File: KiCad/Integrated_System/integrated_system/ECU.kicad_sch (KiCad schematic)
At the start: 49 parts, among them J1 Jack-DC, J2 Fan 1, J3 Fan 2, J4 Fan 3, Q1 BSS138, Q2 BSS138, Q3 BSS138, SW1 SW_SPDT, SW2 SW_SPDT, SW3 SW_Push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

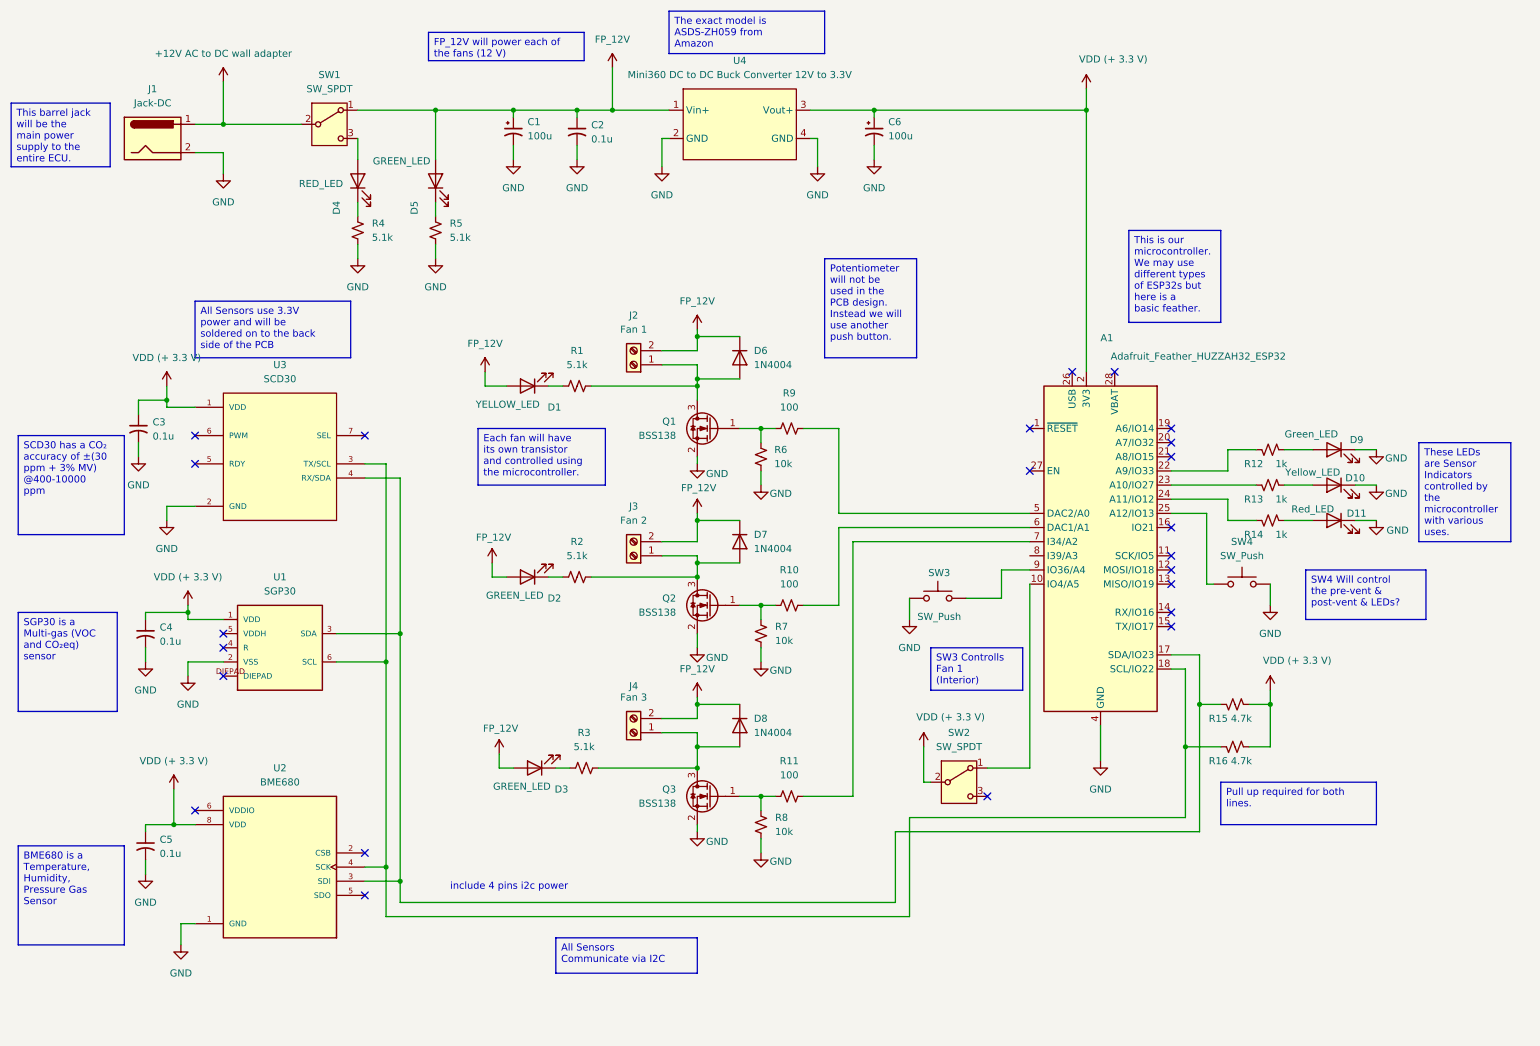
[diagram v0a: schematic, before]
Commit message: added zero ojm resistors and testpoints
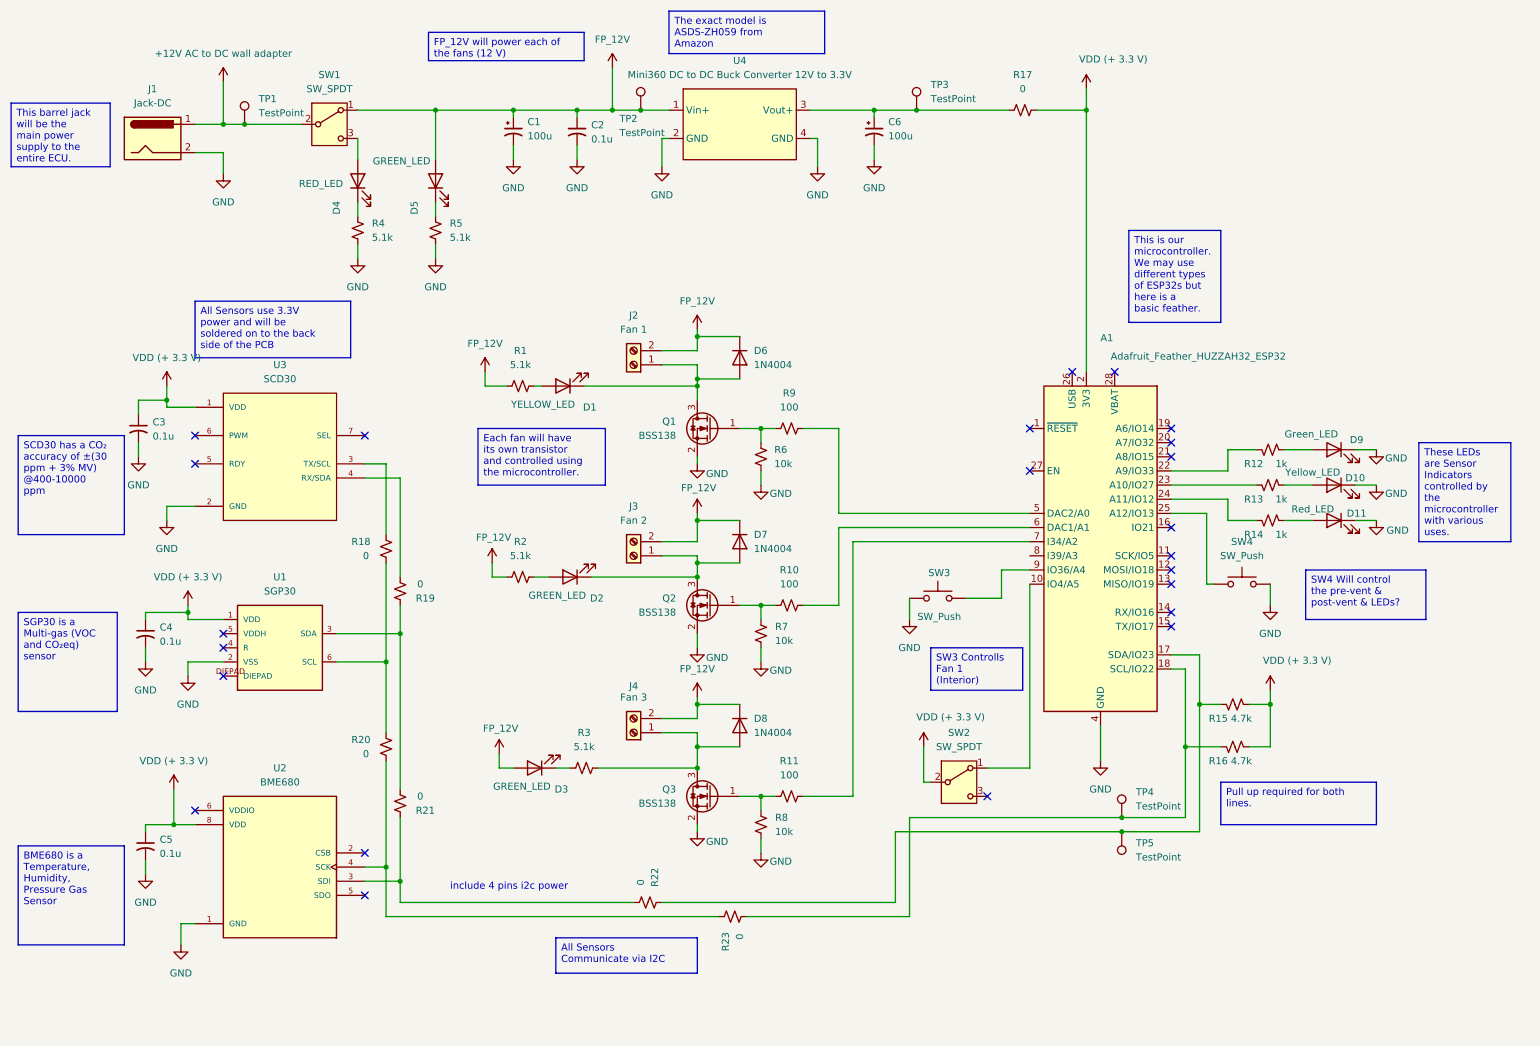
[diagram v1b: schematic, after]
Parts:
- added R17, R18, R19, R20, R21, R22, R23: 0, Resistor_SMD:R_1206_3216Metric_Pad1.30x1.75mm_HandSolder, symbol Device:R_Small_US
- added TP1, TP2, TP3, TP4, TP5: TestPoint, Connector_Pin:Pin_D0.7mm_L6.5mm_W1.8mm_FlatFork, symbol Connector:TestPoint
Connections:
- net +12V AC to DC wall adapter: now also TP1.1
- net FP_12V: now also R1.1, R2.1, TP2.1; no longer D1.2 (A), D2.2 (A)
- net VDD (+ 3.3 V): now also R17.2; no longer C6.1, U4.3 (Vout+)
- net at D6.2 (A), J2.1 (Pin_1), Q1.3 (D): now also D1.1 (K); no longer R1.2
- net at D2.1 (K): now also D7.2 (A), J3.1 (Pin_1), Q2.3 (D); no longer R2.1
- new net: A1.18 (SCL/IO22), R16.2, R23.2, TP4.1
- new net: R19.1, R21.2, U1.3 (SDA)
- new net: R18.2, R20.1, U1.6 (SCL)
- new net: A1.17 (SDA/IO23), R15.2, R22.1, TP5.1
- new net: R21.1, R22.2, U2.3 (SDI)
- new net: D1.2 (A), R1.2
- new net: D2.2 (A), R2.2
- new net: R18.1, U3.3 (TX/SCL)
- new net: R19.2, U3.4 (RX/SDA)
- new net: C6.1, R17.1, TP3.1, U4.3 (Vout+)
- new net: R20.2, R23.1, U2.4 (SCK)
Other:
- moved on the sheet: D1, D2, R1, R2

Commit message: added I2C extension
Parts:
- removed R18, R19, R20, R21, R22, R23: 0, Resistor_SMD:R_1206_3216Metric_Pad1.30x1.75mm_HandSolder, symbol Device:R_Small_US
- added C7: 0.1u, Capacitor_SMD:C_1206_3216Metric_Pad1.33x1.80mm_HandSolder, symbol Device:C_Small_US
- added J5: Conn_01x04, Connector_PinSocket_2.54mm:PinSocket_1x04_P2.54mm_Vertical, symbol Connector_Generic:Conn_01x04
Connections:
- net GND: now also C7.2, J5.3 (Pin_3)
- net VDD (+ 3.3 V): now also C7.1, J5.4 (Pin_4)
- net at A1.18 (SCL/IO22), R16.2, TP4.1: now also U1.6 (SCL), U2.4 (SCK), U3.3 (TX/SCL), J5.2 (Pin_2)
- net at U1.3 (SDA): now also A1.17 (SDA/IO23), R15.2, TP5.1, U2.3 (SDI), U3.4 (RX/SDA), J5.1 (Pin_1)
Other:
- note removed: "include 4 pins i2c power"

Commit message: redesign
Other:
- moved on the sheet: C7
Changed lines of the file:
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@@
 	(text_box "This is our microcontroller. We may use different types of ESP32s but here is a basic feather."
 		(exclude_from_sim no)
-		(at 213.36 53.34 0)
+		(at 175.26 78.74 0)
 		(size 16.51 16.51)
 		(margins 0.9525 0.9525 0.9525 0.9525)
@@
 	)
 	(junction
+		(at 148.59 185.42)
+		(diameter 0)
+		(color 0 0 0 0)
+	)
+	(junction
 		(at 135.89 176.53)
 		(diameter 0)
@@
 	)
 	(junction
-		(at 148.59 182.88)
-		(diameter 0)
-		(color 0 0 0 0)
-	)
-	(junction
 		(at 135.89 115.57)
 		(diameter 0)
@@
 	(wire
 		(pts
-			(xy 163.83 184.15) (xy 163.83 182.88)
-		)
-		(stroke
-			(width 0)
-			(type default)
-		)
-	)
-	(wire
-		(pts
 			(xy 135.89 113.03) (xy 143.51 113.03)
 		)
@@
 	(wire
 		(pts
+			(xy 148.59 193.04) (xy 148.59 194.31)
+		)
+		(stroke
+			(width 0)
+			(type default)
+		)
+	)
+	(wire
+		(pts
 			(xy 135.89 81.28) (xy 135.89 83.82)
 		)
@@
 	(wire
 		(pts
-			(xy 100.33 147.32) (xy 100.33 149.86)
+			(xy 148.59 185.42) (xy 148.59 187.96)
 		)
 		(stroke
@@
 	(wire
 		(pts
-			(xy 43.18 177.8) (xy 45.72 177.8)
+			(xy 100.33 147.32) (xy 100.33 149.86)
 		)
 		(stroke
@@
 	(wire
 		(pts
-			(xy 231.14 96.52) (xy 231.14 92.71)
+			(xy 43.18 177.8) (xy 45.72 177.8)
 		)
 		(stroke
@@
 	(wire
 		(pts
-			(xy 148.59 182.88) (xy 163.83 182.88)
+			(xy 231.14 96.52) (xy 231.14 92.71)
 		)
 		(stroke
@@
 	(wire
 		(pts
-			(xy 163.83 189.23) (xy 163.83 191.77)
-		)
-		(stroke
-			(width 0)
-			(type default)
-		)
-	)
-	(wire
-		(pts
 			(xy 106.68 81.28) (xy 107.95 81.28)
 		)
@@
 	(symbol
 		(lib_id "Device:C_Small_US")
-		(at 163.83 186.69 0)
+		(at 148.59 190.5 0)
 		(unit 1)
 		(exclude_from_sim no)
@@
 		(fields_autoplaced yes)
 		(property "Reference" "C7"
-			(at 166.37 185.5469 0)
+			(at 151.13 189.3569 0)
 			(effects
 				(font
@@
 		)
 		(property "Value" "0.1u"
-			(at 166.37 188.0869 0)
+			(at 151.13 191.8969 0)
 			(effects
 				(font
@@
 		)
 		(property "Footprint" "Capacitor_SMD:C_1206_3216Metric_Pad1.33x1.80mm_HandSolder"
-			(at 163.83 186.69 0)
+			(at 148.59 190.5 0)
 			(effects
 				(font
@@
 		)
 		(property "Datasheet" ""
-			(at 163.83 186.69 0)
+			(at 148.59 190.5 0)
 			(effects
 				(font
@@
 		)
 		(property "Description" "capacitor, small US symbol"
-			(at 163.83 186.69 0)
+			(at 148.59 190.5 0)
 			(effects
 				(font
@@
 	(symbol
 		(lib_id "power:GND")
-		(at 163.83 191.77 0)
+		(at 148.59 194.31 0)
 		(unit 1)
 		(exclude_from_sim no)
@@
 		(dnp no)
 		(property "Reference" "#PWR014"
-			(at 163.83 198.12 0)
+			(at 148.59 200.66 0)
 			(effects
 				(font
@@
 		)
 		(property "Value" "GND"
-			(at 167.894 193.294 0)
+			(at 152.654 195.834 0)
 			(effects
 				(font
@@
 		)
 		(property "Footprint" ""
-			(at 163.83 191.77 0)
+			(at 148.59 194.31 0)
 			(effects
 				(font
@@
 		)
 		(property "Datasheet" ""
-			(at 163.83 191.77 0)
+			(at 148.59 194.31 0)
 			(effects
 				(font
@@
 		)
 		(property "Description" "Power symbol creates a global label with name \"GND\" , ground"
-			(at 163.83 191.77 0)
+			(at 148.59 194.31 0)
 			(effects
 				(font
@@
 		)
 		(property "Value" "GND"
-			(at 144.78 190.5 0)
+			(at 141.224 193.802 0)
 			(effects
 				(font

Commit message: small adjustments
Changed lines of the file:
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@@
 		)
 	)
+	(text_box "Might do a switch instead of a zero ohm resistor to bifuracte the power to the ESP32"
+		(exclude_from_sim no)
+		(at 180.34 34.29 0)
+		(size 21.59 12.7)
+		(margins 0.9525 0.9525 0.9525 0.9525)
+		(stroke
+			(width 0)
+			(type solid)
+		)
+		(fill
+			(type none)
+		)
+		(effects
+			(font
+				(size 1.27 1.27)
+			)
+			(justify left top)
+		)
+	)
 	(text_box "The exact model is ASDS-ZH059 from Amazon"
 		(exclude_from_sim no)
@@
 		(on_board yes)
 		(dnp no)
-		(fields_autoplaced yes)
 		(property "Reference" "TP5"
 			(at 214.63 163.3219 0)
@@
 		)
 		(property "Value" "TestPoint"
-			(at 214.63 165.8619 0)
+			(at 202.184 163.068 0)
 			(effects
 				(font

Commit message: title
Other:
- company: OSSEM -> OSSEM (Open-Source Smart Espresso Machine)
- title: Integrated System -> Integrated ECU System
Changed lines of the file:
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@@
 	(paper "A4")
 	(title_block
-		(title "Integrated System")
-		(date "2026-04-22")
-		(rev "1.3")
-		(company "OSSEM")
+		(title "Integrated ECU System")
+		(date "2026-04-23")
+		(rev "1.4")
+		(company "OSSEM (Open-Source Smart Espresso Machine)")
+		(comment 1 "EE Hardware Engineers: David Mazhnikov, Roman Sulza")
 	)
 	(text_box "These LEDs are Sensor Indicators controlled by the microcontroller with various uses."

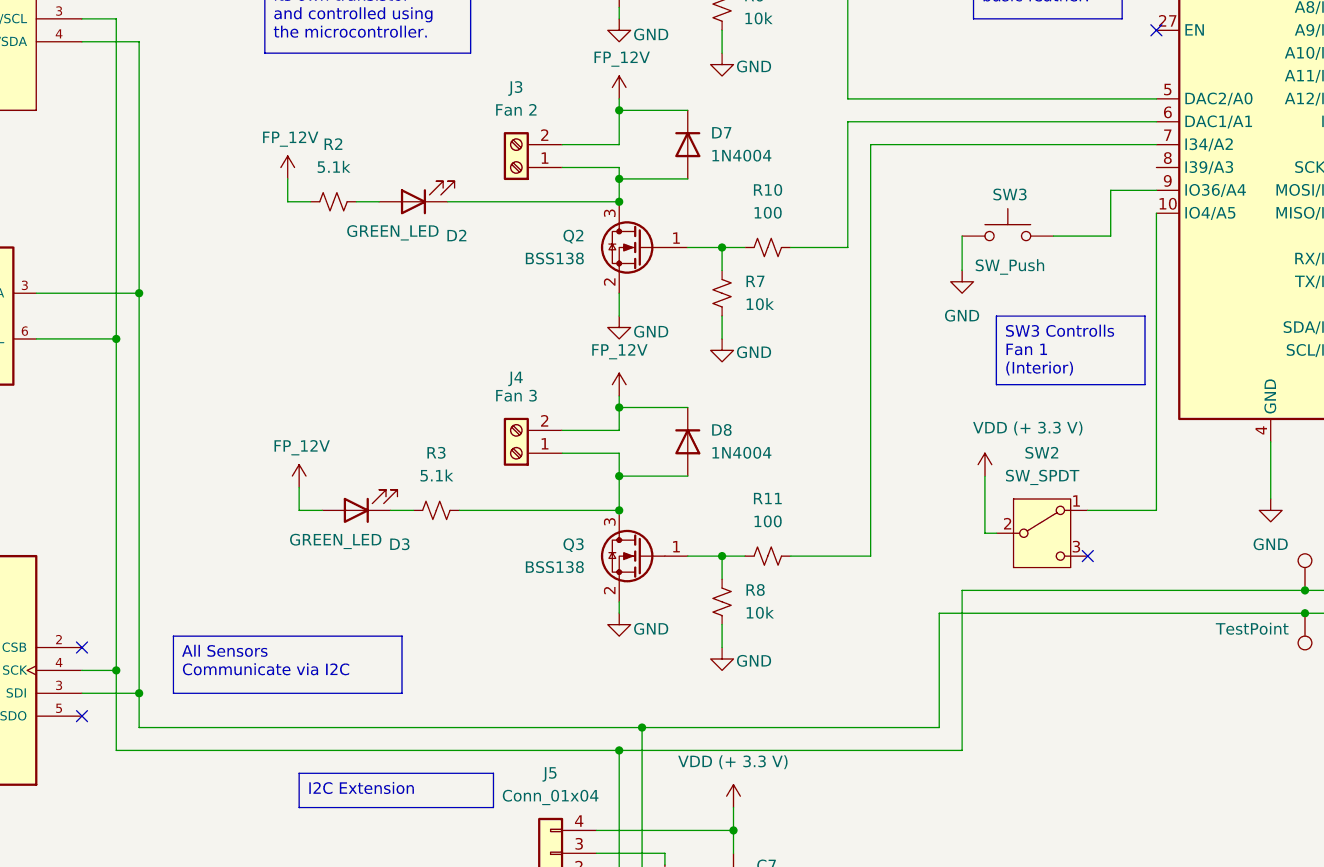
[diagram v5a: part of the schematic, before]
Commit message: Routing Complete
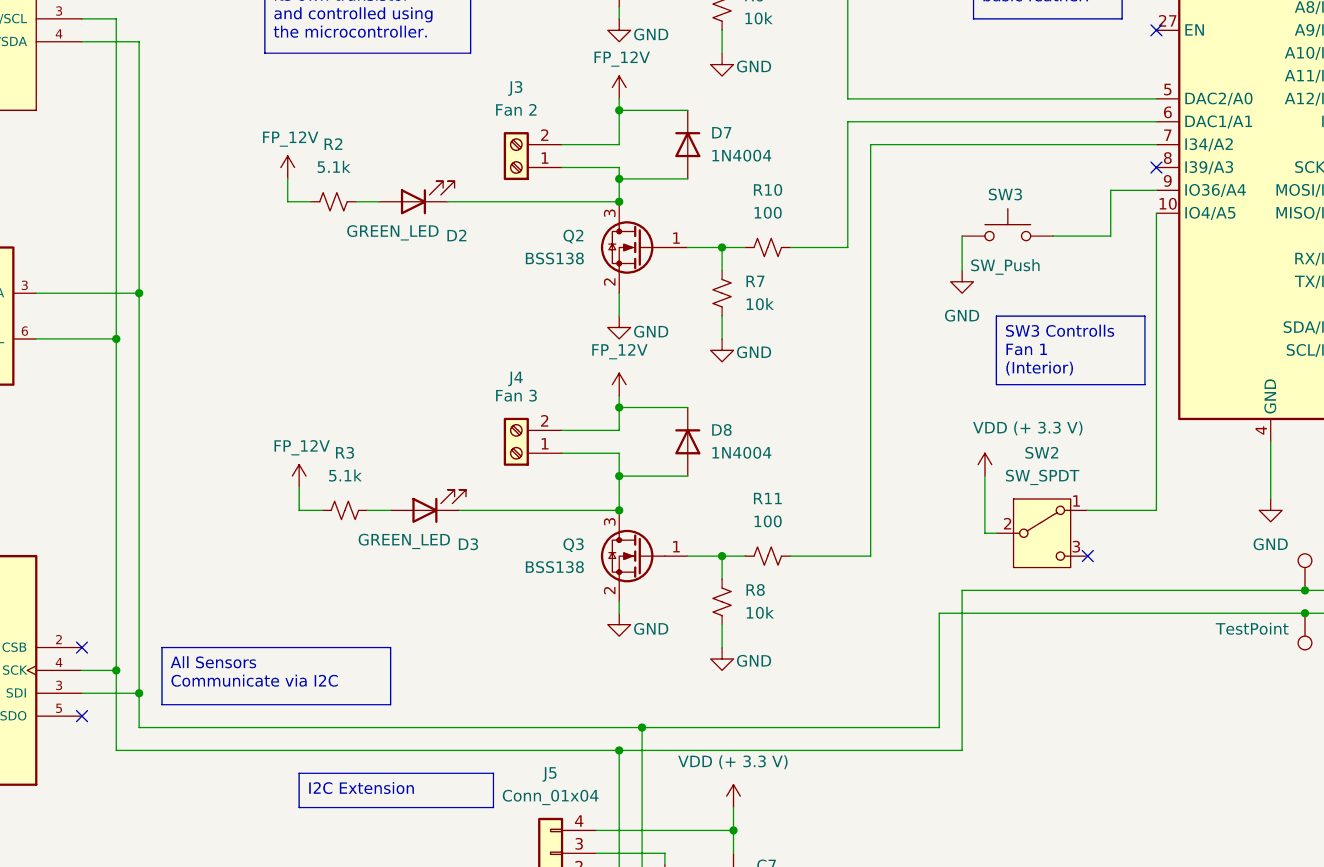
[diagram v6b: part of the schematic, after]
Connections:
- net FP_12V: now also R3.1; no longer D3.2 (A)
- net GND: now also SW3.2; no longer SW3.1
- net at D8.2 (A), J4.1 (Pin_1), Q3.3 (D): now also D3.1 (K); no longer R3.2
- net at A1.9 (IO36/A4): now also SW3.1; no longer SW3.2
- new net: D3.2 (A), R3.2
- no-connect marks 23 -> 24
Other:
- moved on the sheet: D3, R3
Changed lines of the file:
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@@
 	(text_box "All Sensors Communicate via I2C"
 		(exclude_from_sim no)
-		(at 86.36 163.83 0)
+		(at 85.09 165.1 0)
 		(size 25.4 6.35)
 		(margins 0.9525 0.9525 0.9525 0.9525)
@@
 	)
 	(no_connect
+		(at 195.58 111.76)
+	)
+	(no_connect
 		(at 195.58 96.52)
 	)
@@
 	(wire
 		(pts
-			(xy 110.49 149.86) (xy 113.03 149.86)
-		)
-		(stroke
-			(width 0)
-			(type default)
-		)
-	)
-	(wire
-		(pts
 			(xy 129.54 77.47) (xy 135.89 77.47)
 		)
@@
 	(wire
 		(pts
-			(xy 195.58 149.86) (xy 195.58 116.84)
-		)
-		(stroke
-			(width 0)
-			(type default)
-		)
-	)
-	(wire
-		(pts
 			(xy 148.59 182.88) (xy 148.59 185.42)
 		)
@@
 	(wire
 		(pts
+			(xy 195.58 116.84) (xy 195.58 149.86)
+		)
+		(stroke
+			(width 0)
+			(type default)
+		)
+	)
+	(wire
+		(pts
 			(xy 161.29 120.65) (xy 161.29 106.68)
 		)
@@
 	(wire
 		(pts
+			(xy 107.95 149.86) (xy 110.49 149.86)
+		)
+		(stroke
+			(width 0)
+			(type default)
+		)
+	)
+	(wire
+		(pts
 			(xy 135.89 176.53) (xy 80.01 176.53)
 		)
@@
 		(lib_id "Switch:SW_Push")
 		(at 179.07 119.38 0)
+		(mirror y)
 		(unit 1)
 		(exclude_from_sim no)
@@
 		(dnp no)
 		(property "Reference" "SW3"
-			(at 179.324 114.808 0)
+			(at 178.816 114.808 0)
 			(effects
 				(font
@@
 		)
 		(property "Value" "SW_Push"
-			(at 179.324 122.682 0)
+			(at 178.816 122.682 0)
 			(effects
 				(font
@@
 	(symbol
 		(lib_id "Device:LED")
-		(at 106.68 149.86 180)
+		(at 114.3 149.86 180)
 		(unit 1)
 		(exclude_from_sim no)
@@
 		(dnp no)
 		(property "Reference" "D3"
-			(at 111.506 153.67 0)
+			(at 119.126 153.67 0)
 			(effects
 				(font
@@
 		)
 		(property "Value" "GREEN_LED"
-			(at 104.394 153.162 0)
+			(at 112.014 153.162 0)
 			(effects
 				(font
@@
 		)
 		(property "Footprint" "LED_SMD:LED_1206_3216Metric_Pad1.42x1.75mm_HandSolder"
-			(at 106.68 149.86 0)
+			(at 114.3 149.86 0)
 			(effects
 				(font
@@
 		)
 		(property "Datasheet" "~"
-			(at 106.68 149.86 0)
+			(at 114.3 149.86 0)
 			(effects
 				(font
@@
 		)
 		(property "Description" "Light emitting diode"
-			(at 106.68 149.86 0)
+			(at 114.3 149.86 0)
 			(effects
 				(font
@@
 		)
 		(property "Sim.Pins" "1=K 2=A"
-			(at 106.68 149.86 0)
+			(at 114.3 149.86 0)
 			(effects
 				(font
@@
 				)
 			)
-			(project "integrated_system"
-				(path "/e09e0073-4b34-4087-926d-a963f587ec36/d64a58e5-7375-438d-b343-064b897cc797"
-					(reference "D?")
-					(unit 1)
-				)
-			)
 		)
 	)
@@
 	(symbol
 		(lib_id "Device:R_Small_US")
-		(at 115.57 149.86 90)
+		(at 105.41 149.86 90)
 		(unit 1)
 		(exclude_from_sim no)
@@
 		(fields_autoplaced yes)
 		(property "Reference" "R3"
-			(at 115.57 143.51 90)
+			(at 105.41 143.51 90)
 			(effects
 				(font
@@
 		)
 		(property "Value" "5.1k"
-			(at 115.57 146.05 90)
+			(at 105.41 146.05 90)
 			(effects
 				(font
@@
 		)
 		(property "Footprint" "Resistor_SMD:R_1206_3216Metric_Pad1.30x1.75mm_HandSolder"
-			(at 115.57 149.86 0)
+			(at 105.41 149.86 0)
 			(effects
 				(font
@@
 		)
 		(property "Datasheet" "~"
-			(at 115.57 149.86 0)
+			(at 105.41 149.86 0)
 			(effects
 				(font
@@
 		)
 		(property "Description" "Resistor, small US symbol"
-			(at 115.57 149.86 0)
+			(at 105.41 149.86 0)
 			(effects
 				(font
@@
 				)
 			)
-			(project "integrated_system"
-				(path "/e09e0073-4b34-4087-926d-a963f587ec36/d64a58e5-7375-438d-b343-064b897cc797"
-					(reference "R?")
-					(unit 1)
-				)
-			)
 		)
 	)
@@
 		(on_board yes)
 		(dnp no)
-		(fields_autoplaced yes)
 		(property "Reference" "J3"
 			(at 124.46 102.87 0)
@@
 		(on_board yes)
 		(dnp no)
-		(fields_autoplaced yes)
 		(property "Reference" "SW2"
 			(at 182.88 143.51 0)

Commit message: headers
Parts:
- removed J5: Conn_01x04, Connector_PinSocket_2.54mm:PinSocket_1x04_P2.54mm_Vertical, symbol Connector_Generic:Conn_01x04
- added J6: Conn_02x04_Counter_Clockwise, Connector_PinSocket_2.54mm:PinSocket_2x04_P2.54mm_Vertical, symbol Connector_Generic:Conn_02x04_Counter_Clockwise
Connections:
- net GND: now also J6.5 (Pin_5), J6.6 (Pin_6)
- net VDD (+ 3.3 V): now also J6.7 (Pin_7), J6.8 (Pin_8)
- net at A1.17 (SDA/IO23), R15.2, TP5.1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: now also J6.1 (Pin_1), J6.2 (Pin_2)
- net at A1.18 (SCL/IO22), R16.2, TP4.1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: now also J6.3 (Pin_3), J6.4 (Pin_4)
